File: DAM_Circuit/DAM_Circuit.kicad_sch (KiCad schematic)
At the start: 60 parts, among them U1 74LS147, U10 74LS48, U11 74LS125, U12 74LS20, U13 74LS21, U14 74LS85, U15 74LS85, U16 74LS32, U17 A1104xLH, U18 A1104xLH, U19 A1104xLH, U2 74LS175, U20 A1104xLH, U21 A1104xLH, U22 A1104xLH, U23 A1104xLH, U24 A1104xLH, U25 A1104xLH, U26 A1104xLH, U3 74LS157, U4 74LS85, U5 74LS04, U6 74LS32, U7 74LS04, U8 74LS85, U9 74LS157

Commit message: 6.6.2026 --updated pcb
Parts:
- added BZ1: Buzzer, TerminalBlock_Phoenix:TerminalBlock_Phoenix_MKDS-1,5-2_1x02_P5.00mm_Horizontal, symbol Device:Buzzer
- added C15, C16, C17, C18: 100 nF, symbol Device:C
- added D1, D2: 1N4007, Diode_THT:D_DO-41_SOD81_P10.16mm_Horizontal, symbol Diode:1N4007
- added J1, J2: Screw_Terminal_01x02, TerminalBlock_Phoenix:TerminalBlock_Phoenix_MKDS-1,5-2_1x02_P5.00mm_Horizontal, symbol Connector:Screw_Terminal_01x02
- added Q1, Q2: IRLZ44N, Package_TO_SOT_THT:TO-220-3_Vertical, symbol Transistor_FET:IRLZ44N
- added R21, R22, R23, R24, R25, R26, R27, R28, R29, R30, R31, R32, R33: 330R, Resistor_THT:R_Axial_DIN0207_L6.3mm_D2.5mm_P10.16mm_Horizontal, symbol Device:R
- added R34, R35, R36, R39: 10K, Resistor_THT:R_Axial_DIN0207_L6.3mm_D2.5mm_P10.16mm_Horizontal, symbol Device:R
- added R37, R38: 100R, Resistor_THT:R_Axial_DIN0207_L6.3mm_D2.5mm_P10.16mm_Horizontal, symbol Device:R
- added SW1, SW2: SW_Push, Button_Switch_THT:SW_PUSH_6mm_H5mm, symbol Switch:SW_Push
- added U27, U28: SM420561N, Display_7Segment:7SegmentLED_LTS6760_LTS6780, symbol Display_Character:SM420561N
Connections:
- net VCC is gone; now on net +5V: C1.1, C10.2, C11.2, C12.2, C13.2, C14.2, C2.2, C3.2, C4.1, C5.2, C6.2, C7.2, C8.2, C9.2, R1.1, R11.1, R13.1, R15.1, R17.1, R19.1, R3.1, R5.1, R7.1, R9.1, U1.16 (VCC), U10.16 (VCC), U11.14 (VCC), U12.14 (VCC), U13.14 (VCC), U16.14 (VCC), U17.1 (V_{CC}), U18.1 (V_{CC}), U19.1 (V_{CC}), U2.1 (~{Mr}), U2.16 (VCC), U20.1 (V_{CC}), U21.1 (V_{CC}), U22.1 (V_{CC}), U23.1 (V_{CC}), U24.1 (V_{CC}), U25.1 (V_{CC}), U26.1 (V_{CC}), U3.10 (I1c), U3.16 (VCC), U3.3 (I1a), U4.16 (VCC), U4.3 (Ia=b), U5.14 (VCC), U6.14 (VCC), U7.14 (VCC), U8.1 (B3), U8.16 (VCC), U8.3 (Ia=b), U8.9 (B0), U9.16 (VCC)
- net A: now also U14.10 (A0), U15.10 (A0)
- net B: now also U14.12 (A1), U15.12 (A1)
- net C: now also U14.13 (A2), U15.13 (A2)
- net D: now also U14.15 (A3), U15.15 (A3)
- net GND: now also U11.12, U11.9, U14.11 (B1), U14.14 (B2), U14.2 (Ia<b), U14.4 (Ia>b), U14.8 (GND), U14.9 (B0), U15.1 (B3), U15.11 (B1), U15.2 (Ia<b), U15.4 (Ia>b), U15.8 (GND), U15.9 (B0), U7.11, U7.13, U7.9, BZ1.2 (-), C15.1, C16.1, C17.2, C18.2, Q1.3 (S), Q2.3 (S), R34.2, R35.2, R36.2, R39.2, U27.3 (CC), U27.8 (CC), U28.3 (CC), U28.8 (CC)
- net at U16.10: now also C17.1, R34.1, SW1.2
- net at U16.8: now also R37.1
- net at U16.9: now also U16.3
- net at U16.4: now also U15.5 (Oa>b)
- net at U16.5: now also U15.6 (Oa=b)
- net at U16.6: now also U16.12
- net +5V: now reaches U15.14 (B2)
- net +5V: now also U10.3 (LT), U10.4 (BI), U10.5 (RBI), U14.1 (B3), U14.16 (VCC), U14.3 (Ia=b), U15.16 (VCC), U15.3 (Ia=b), C15.2, C16.2, R29.2, R30.2, SW1.1, SW2.1
- net at U10.1 (B): now also U9.7 (Zb)
- net at U10.10 (d): now also R24.2
- net at U10.11 (c): now also R23.2
- net at U10.12 (b): now also R22.2
- net at U10.13 (a): now also R21.2
- net at U10.14 (g): now also R27.2
- net at U10.15 (f): now also R26.2
- net at U10.2 (C): now also U9.9 (Zc)
- net at U10.6 (D): now also U9.12 (Zd)
- net at U10.7 (A): now also U9.4 (Za)
- net at U10.9 (e): now also R25.2
- net at U14.5 (Oa>b): now also U16.1
- net at U14.6 (Oa=b): now also U16.2
- net at U7.5: now also U11.2, U12.8
- net at U7.6: now also U11.5
- net at U11.3: now also R28.2, R31.2, R32.2, R33.2
- net at U16.11: now also R38.1
- net at U16.13: now also C18.1, R35.1, SW2.2
- net at U11.6: now also BZ1.1 (+)
- new net: Q2.1 (G), R38.2, R39.1
- new net: R28.1, U28.7 (A)
- new net: R22.1, U27.6 (B)
- new net: R33.1, U28.9 (F)
- new net: R24.1, U27.2 (D)
- new net: R25.1, U27.1 (E)
- new net: R27.1, U27.10 (G)
- new net: Q1.1 (G), R36.1, R37.2
- new net: D2.2 (A), J2.2 (Pin_2), Q2.2 (D)
- new net: R23.1, U27.4 (C)
- new net: R21.1, U27.7 (A)
- new net: R26.1, U27.9 (F)
- new net: D1.2 (A), J1.2 (Pin_2), Q1.2 (D)
- new net: R30.1, U28.4 (C)
- new net: R32.1, U28.1 (E)
- new net: R31.1, U28.2 (D)
- new net: R29.1, U28.6 (B)
- new net +12V: D1.1 (K), D2.1 (K), J1.1 (Pin_1), J2.1 (Pin_1)
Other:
- moved on the sheet: C11, C12, C13, C14, U10, U11A, U11B, U11C, U11D, U11E, U16A, U16B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

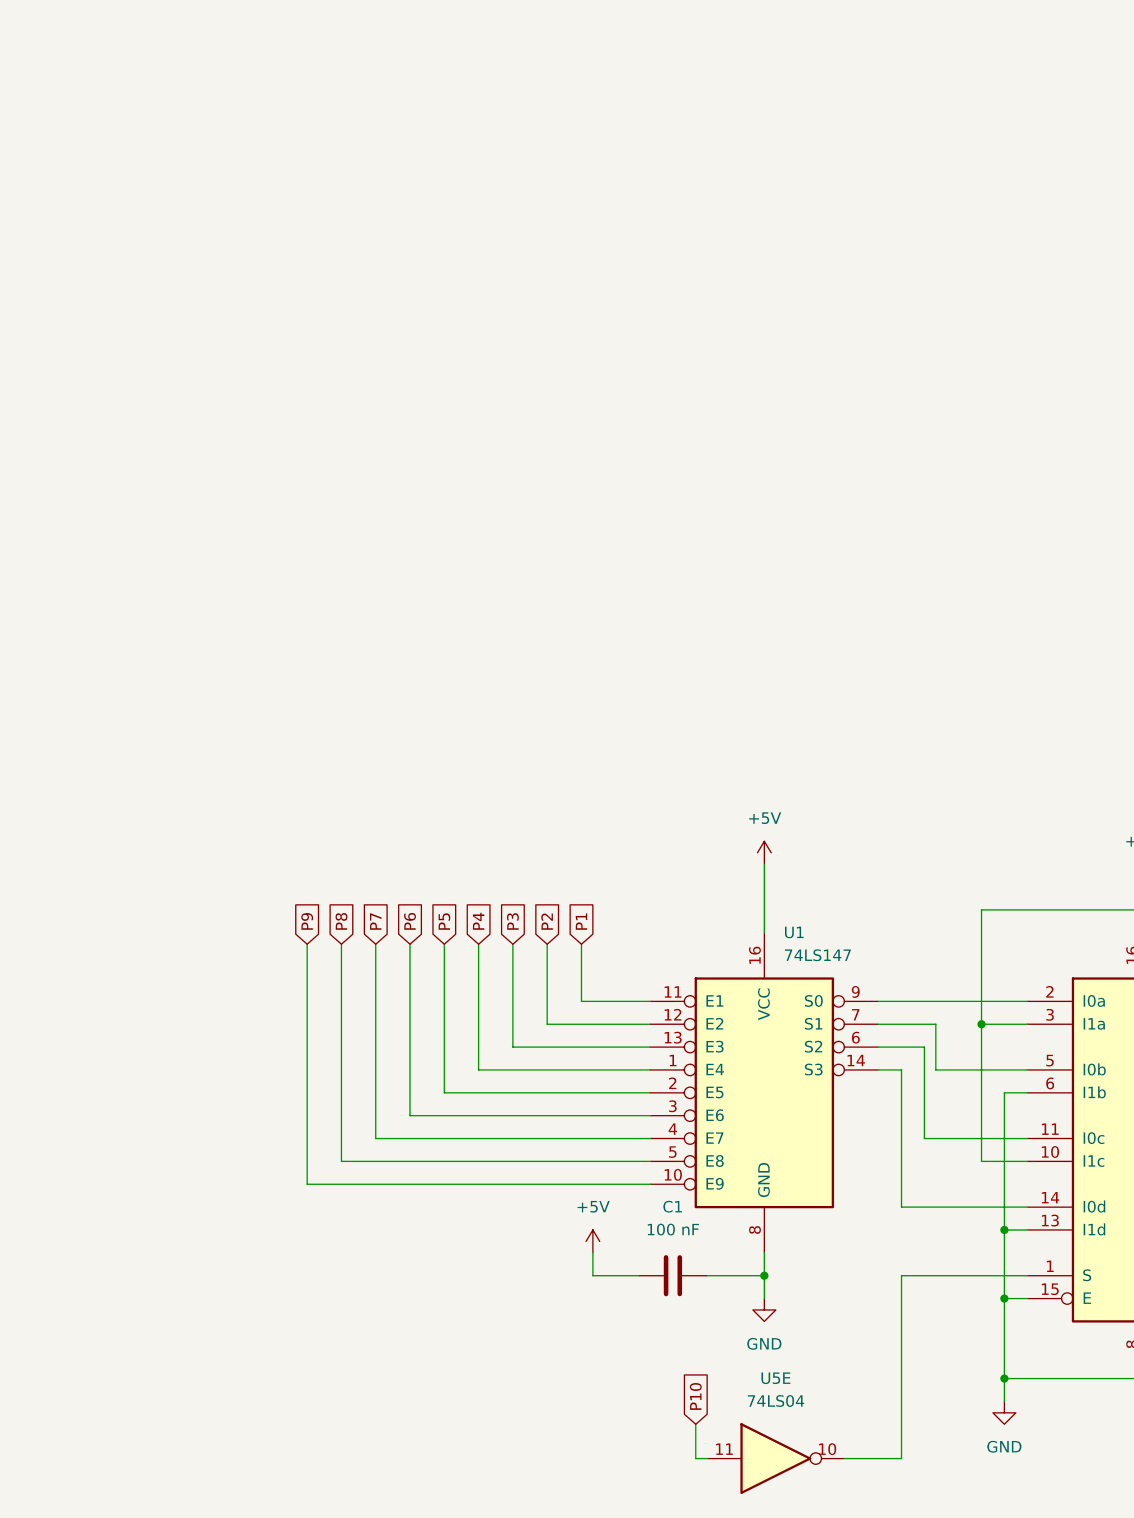
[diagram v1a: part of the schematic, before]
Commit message: 6.6.2026 finalized schematic
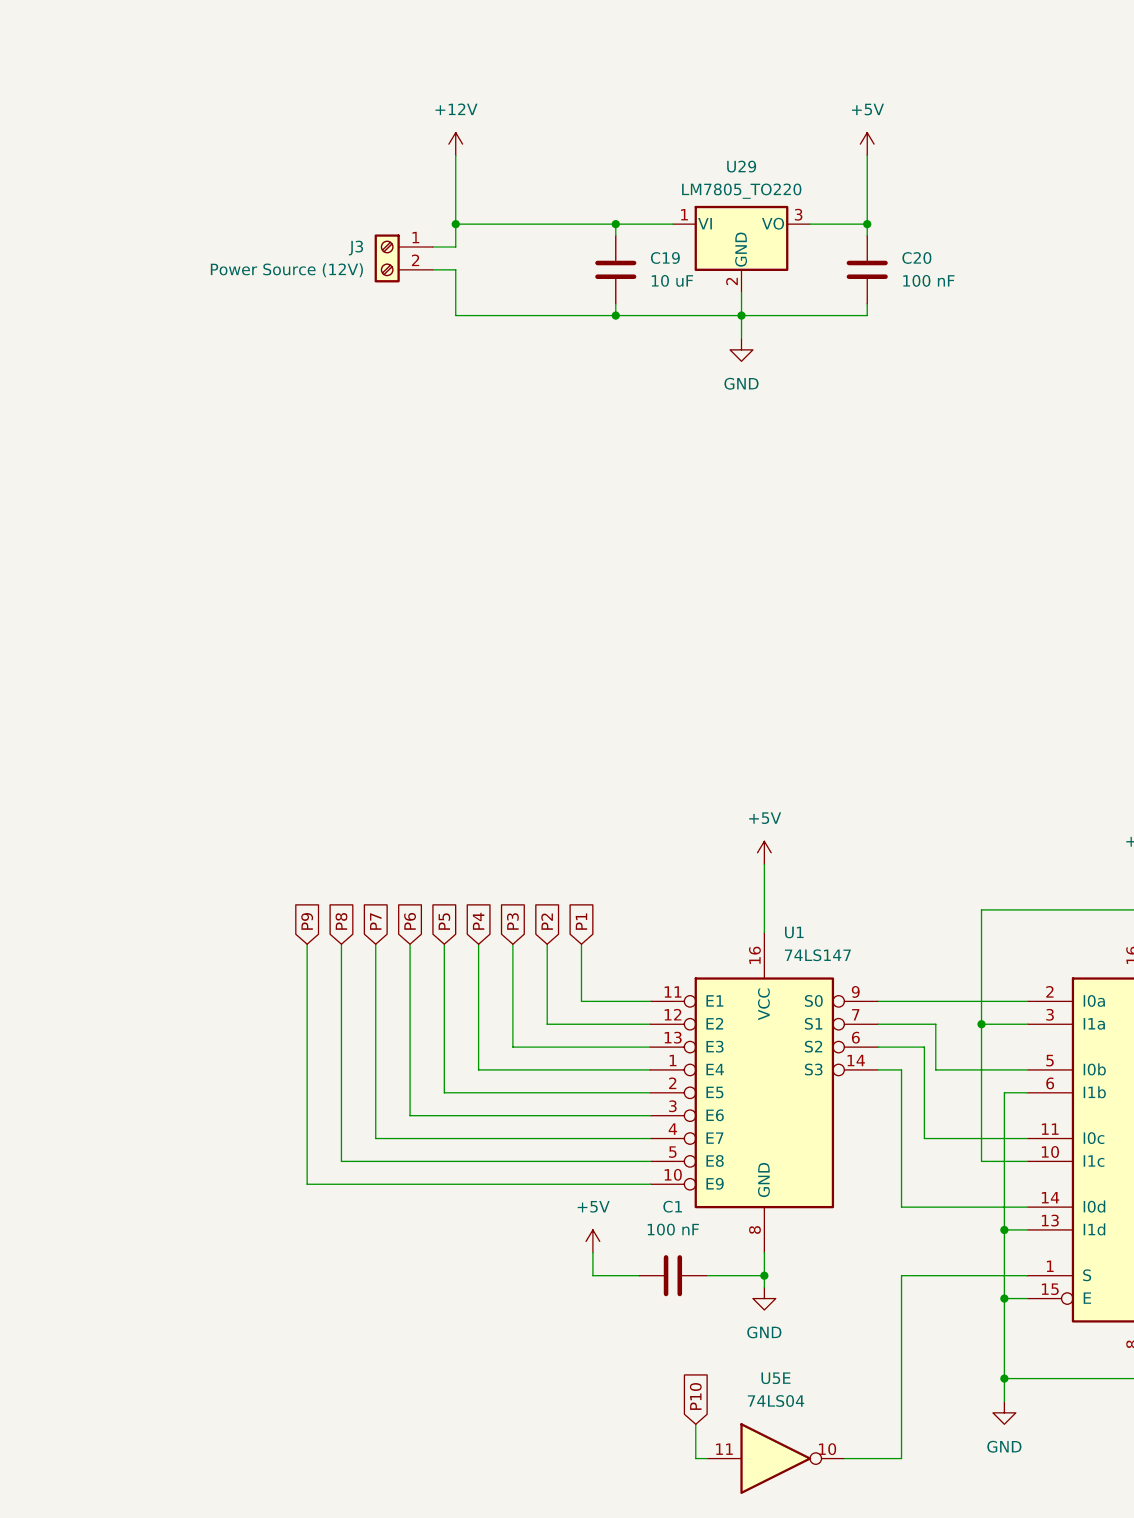
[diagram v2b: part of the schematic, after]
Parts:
- added C19: 10 uF, Capacitor_THT:C_Disc_D5.0mm_W2.5mm_P5.00mm, symbol Device:C
- added C20: 100 nF, Capacitor_THT:C_Disc_D5.0mm_W2.5mm_P5.00mm, symbol Device:C
- added J3: Power Source (12V), TerminalBlock_Phoenix:TerminalBlock_Phoenix_MKDS-1,5-2_1x02_P5.00mm_Horizontal, symbol Connector:Screw_Terminal_01x02
- added U29: LM7805_TO220, Package_TO_SOT_THT:TO-220-3_Vertical, symbol Regulator_Linear:LM7805_TO220
- C1, C10, C11, C12, C13, C14, C15, C16, C17, C18, C2, C3, C4, C5, C6, C7, C8, C9: footprint (none) -> Capacitor_THT:C_Disc_D5.0mm_W2.5mm_P5.00mm
- U1, U10, U14, U15, U2, U3, U4, U8, U9: footprint (none) -> Package_DIP:DIP-16_W7.62mm
- U11, U12, U13, U16, U5, U6, U7: footprint (none) -> Package_DIP:DIP-14_W7.62mm
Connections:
- net +12V: now also C19.2, J3.1 (Pin_1), U29.1 (VI)
- net +5V: now also C20.2, U29.3 (VO)
- net GND: now also C19.1, C20.1, J3.2 (Pin_2), U29.2 (GND)

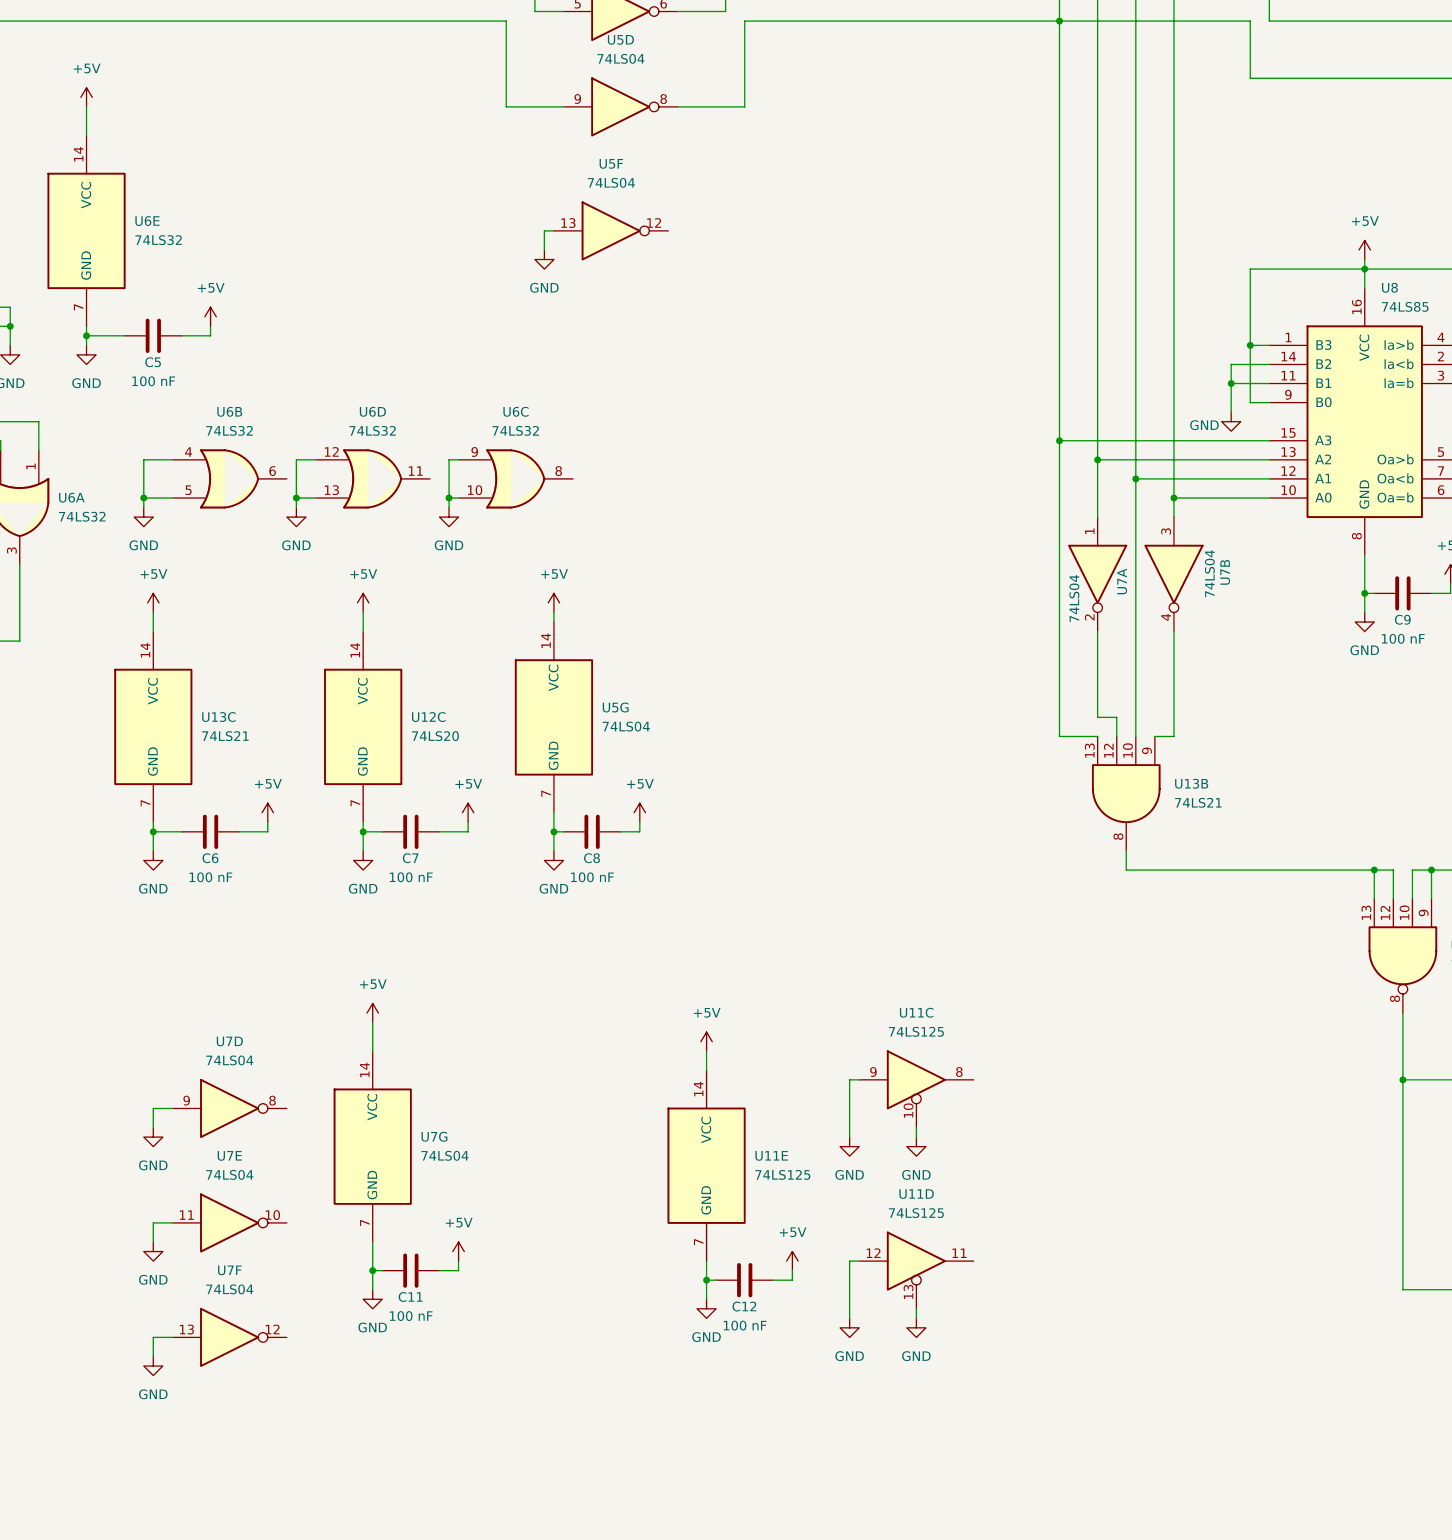
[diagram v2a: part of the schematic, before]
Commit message: 6.7.2026 layout but no routing
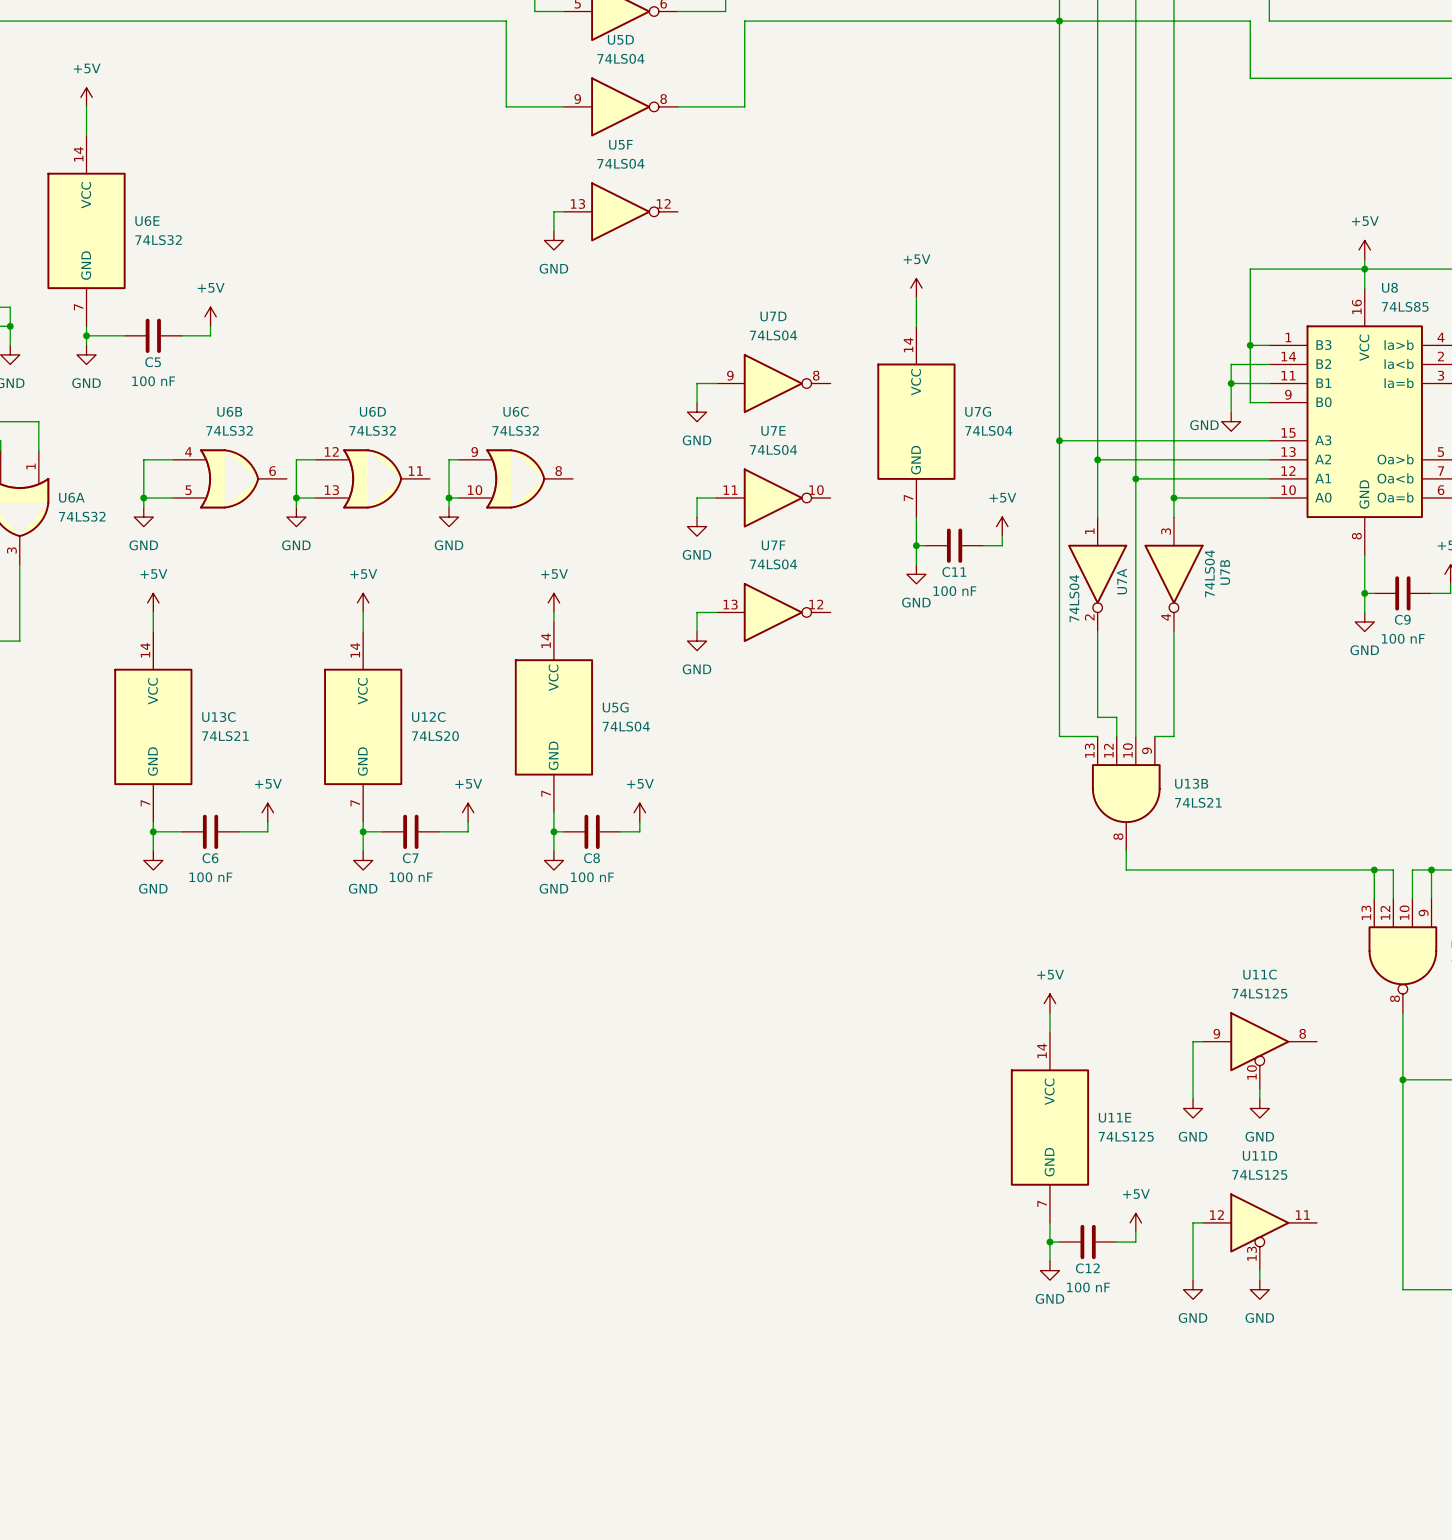
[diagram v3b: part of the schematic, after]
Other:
- moved on the sheet: C11, C12, U11C, U11D, U11E, U5F, U7D, U7E, U7F, U7G
